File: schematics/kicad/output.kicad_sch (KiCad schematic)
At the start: 33 parts, among them J7 DE15_Socket_HighDensity, K1300 10uF, U1300 HM53461, U1301 HM53461, U1302 HM53461, U1303 HM53461, U1304 HM53461, U1305 HM53461, U1306 HM53461, U1307 HM53461, U1310 BT458, U1311 92.9405Mhz, U1312 10H101, U1313 10H131, U1314 10H350, U1315 LM385BZ-1.2, U1318 74F08

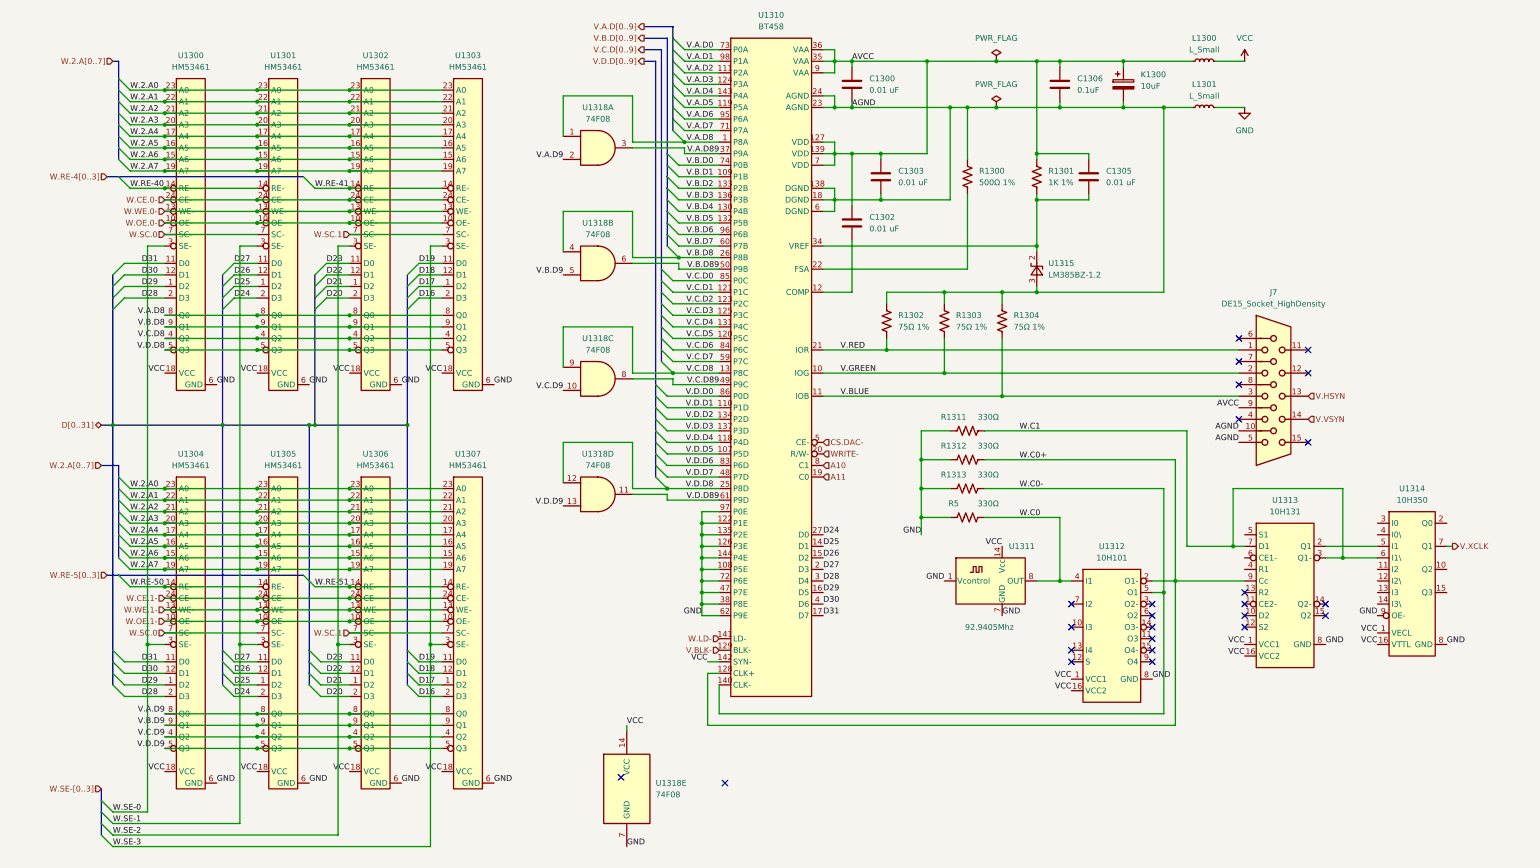
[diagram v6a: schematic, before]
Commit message: Fix ERCs which uncovered some issues with W.RE for the overlay memory. Finish the ECL chips for clock control - need to find value of R1315. Add space for 0-ohm resistor on V.VSYN which exists in schematics but was never connected in the original composite sync scheme with 4 BNC connectors. Can leave it unconnected if it causes issues.
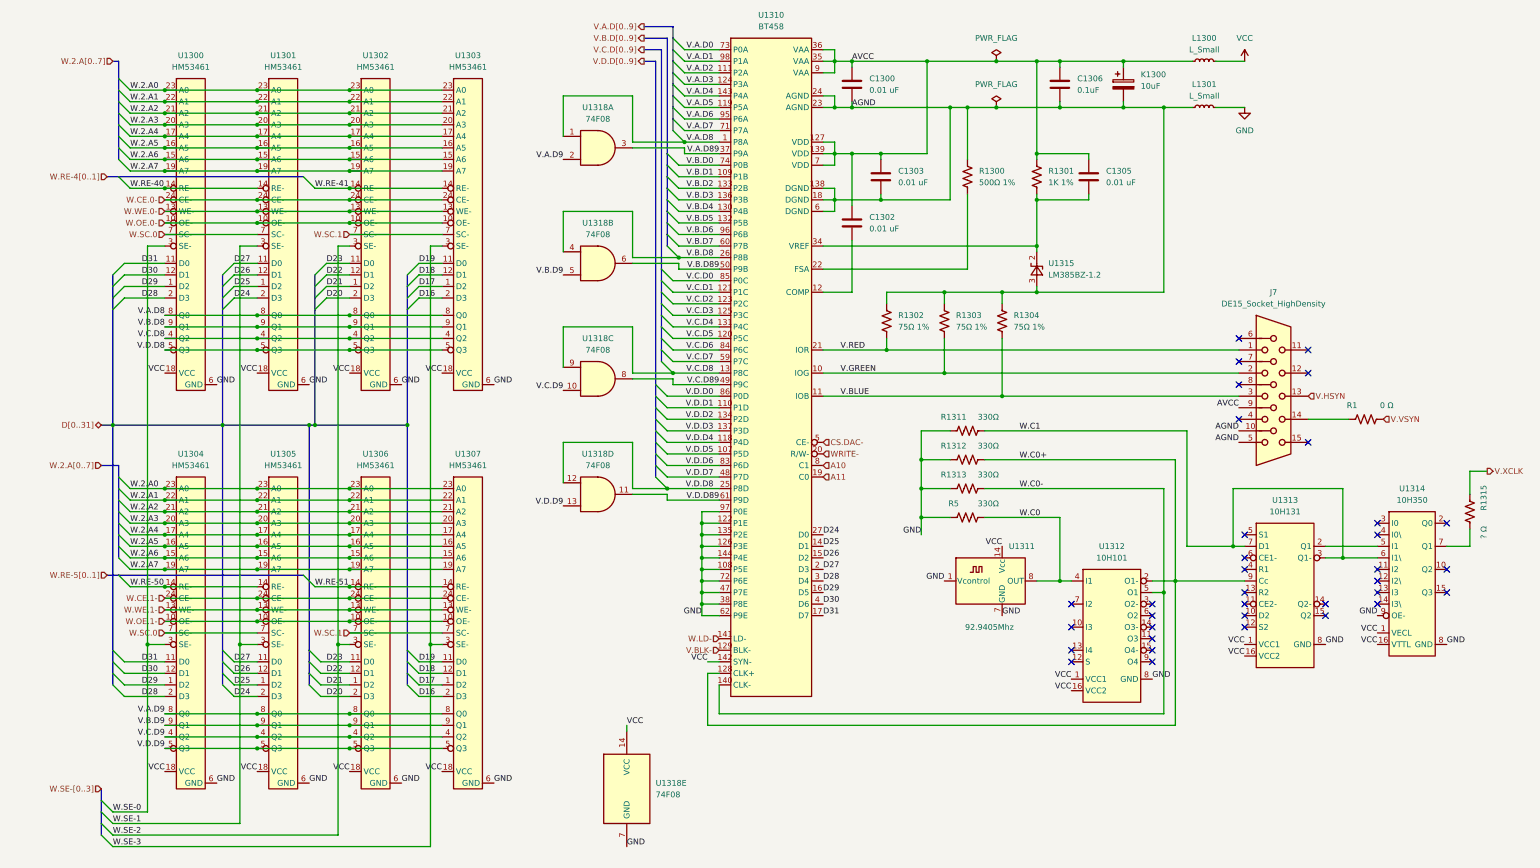
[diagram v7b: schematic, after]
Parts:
- added R1: 0 Ω, Resistor_THT:R_Axial_DIN0207_L6.3mm_D2.5mm_P10.16mm_Horizontal, symbol Device:R_US
- added R1315: ? Ω, Resistor_THT:R_Axial_DIN0207_L6.3mm_D2.5mm_P10.16mm_Horizontal, symbol Device:R_US
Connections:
- net V.VSYN: now also R1.2; no longer J7.14
- net V.XCLK: now also R1315.1; no longer U1314.7 (Q1)
- new net: R1315.2, U1314.7 (Q1)
- new net: J7.14, R1.1
- no-connect marks 25 -> 35
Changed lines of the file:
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@@
 	)
 	(no_connect
-		(at 166.37 182.88)
+		(at 280.67 146.05)
 	)
 	(no_connect
-		(at 280.67 146.05)
+		(at 280.67 135.89)
 	)
 	(no_connect
@@
 	)
 	(no_connect
+		(at 309.88 125.73)
+	)
+	(no_connect
+		(at 309.88 135.89)
+	)
+	(no_connect
+		(at 309.88 140.97)
+	)
+	(no_connect
 		(at 294.64 107.95)
 	)
@@
 	)
 	(no_connect
-		(at 294.64 87.63)
+		(at 309.88 143.51)
 	)
 	(no_connect
-		(at 143.51 181.61)
+		(at 294.64 87.63)
 	)
 	(no_connect
@@
 	)
 	(no_connect
+		(at 280.67 133.35)
+	)
+	(no_connect
 		(at 260.35 151.13)
 	)
@@
 	)
 	(no_connect
+		(at 325.12 125.73)
+	)
+	(no_connect
 		(at 242.57 156.21)
 	)
@@
 	)
 	(no_connect
+		(at 280.67 128.27)
+	)
+	(no_connect
+		(at 309.88 138.43)
+	)
+	(no_connect
 		(at 280.67 143.51)
 	)
@@
 	)
 	(no_connect
+		(at 309.88 128.27)
+	)
+	(no_connect
 		(at 242.57 143.51)
 	)
@@
 	)
 	(no_connect
+		(at 325.12 140.97)
+	)
+	(no_connect
+		(at 325.12 135.89)
+	)
+	(no_connect
 		(at 279.4 90.17)
 	)
@@
 	(wire
 		(pts
+			(xy 303.53 102.87) (xy 294.64 102.87)
+		)
+		(stroke
+			(width 0)
+			(type default)
+		)
+	)
+	(wire
+		(pts
 			(xy 63.5 170.18) (xy 83.82 170.18)
 		)
@@
 	(wire
 		(pts
-			(xy 325.12 130.81) (xy 326.39 130.81)
-		)
-		(stroke
-			(width 0)
-			(type default)
-		)
-	)
-	(wire
-		(pts
 			(xy 157.48 36.83) (xy 165.1 36.83)
 		)
@@
 	(wire
 		(pts
+			(xy 330.2 127) (xy 330.2 130.81)
+		)
+		(stroke
+			(width 0)
+			(type default)
+		)
+	)
+	(wire
+		(pts
 			(xy 43.18 52.07) (xy 63.5 52.07)
 		)
@@
 	(wire
 		(pts
+			(xy 330.2 114.3) (xy 330.2 119.38)
+		)
+		(stroke
+			(width 0)
+			(type default)
+		)
+	)
+	(wire
+		(pts
 			(xy 83.82 35.56) (xy 104.14 35.56)
 		)
@@
 		)
 	)
+	(wire
+		(pts
+			(xy 330.2 114.3) (xy 334.01 114.3)
+		)
+		(stroke
+			(width 0)
+			(type default)
+		)
+	)
 	(bus
 		(pts
@@
 	(wire
 		(pts
+			(xy 325.12 130.81) (xy 330.2 130.81)
+		)
+		(stroke
+			(width 0)
+			(type default)
+		)
+	)
+	(wire
+		(pts
 			(xy 153.67 107.95) (xy 165.1 107.95)
 		)
@@
 		)
 	)
-	(hierarchical_label "W.RE-4[0..3]"
+	(hierarchical_label "V.XCLK"
+		(shape output)
+		(at 334.01 114.3 0)
+		(effects
+			(font
+				(size 1.27 1.27)
+			)
+			(justify left)
+		)
+	)
+	(hierarchical_label "W.RE-4[0..1]"
 		(shape input)
 		(at 30.48 49.53 180)
@@
 		)
 	)
-	(hierarchical_label "V.XCLK"
-		(shape output)
-		(at 326.39 130.81 0)
+	(hierarchical_label "V.VSYN"
+		(shape input)
+		(at 311.15 102.87 0)
 		(effects
 			(font
@@
 		)
 	)
-	(hierarchical_label "V.VSYN"
-		(shape input)
-		(at 294.64 102.87 0)
-		(effects
-			(font
-				(size 1.27 1.27)
-			)
-			(justify left)
-		)
-	)
 	(hierarchical_label "A11"
 		(shape input)
@@
 		)
 	)
-	(hierarchical_label "W.RE-5[0..3]"
+	(hierarchical_label "W.RE-5[0..1]"
 		(shape input)
 		(at 30.48 137.16 180)
@@
 	)
 	(symbol
+		(lib_id "Device:R_US")
+		(at 330.2 123.19 0)
+		(unit 1)
+		(exclude_from_sim no)
+		(in_bom yes)
+		(on_board yes)
+		(dnp no)
+		(property "Reference" "R1315"
+			(at 333.248 120.142 90)
+			(effects
+				(font
+					(size 1.27 1.27)
+				)
+			)
+		)
+		(property "Value" "? Ω"
+			(at 333.248 127.762 90)
+			(effects
+				(font
+					(size 1.27 1.27)
+				)
+			)
+		)
+		(property "Footprint" "Resistor_THT:R_Axial_DIN0207_L6.3mm_D2.5mm_P10.16mm_Horizontal"
+			(at 331.216 123.444 90)
+			(effects
+				(font
+					(size 1.27 1.27)
+				)
+				(hide yes)
+			)
+		)
+		(property "Datasheet" "~"
+			(at 330.2 123.19 0)
+			(effects
+				(font
+					(size 1.27 1.27)
+				)
+				(hide yes)
+			)
+		)
+		(property "Description" "Resistor, US symbol"
+			(at 330.2 123.19 0)
+			(effects
+				(font
+					(size 1.27 1.27)
+				)
+				(hide yes)
+			)
+		)
+		(pin "2"
+		)
+		(pin "1"
+		)
+		(instances
+			(project "cg4"
+				(path "/7c2b6a13-c303-4adb-8eed-6e6a9ac5307e/29ede95e-baf3-44af-bd6e-b3be323fd399"
+					(reference "R1315")
+					(unit 1)
+				)
+			)
+		)
+	)
+	(symbol
 		(lib_id "power:PWR_FLAG")
 		(at 226.06 34.29 0)
@@
 					(unit 1)
 				)
+			)
+		)
+	)
+	(symbol
+		(lib_id "Device:R_US")
+		(at 307.34 102.87 90)
+		(unit 1)
+		(exclude_from_sim no)
+		(in_bom yes)
+		(on_board yes)
+		(dnp no)
+		(property "Reference" "R1"
+			(at 304.292 99.822 90)
+			(effects
+				(font
+					(size 1.27 1.27)
+				)
+			)
+		)
+		(property "Value" "0 Ω"
+			(at 311.912 99.822 90)
+			(effects
+				(font
+					(size 1.27 1.27)
+				)
+			)
+		)
+		(property "Footprint" "Resistor_THT:R_Axial_DIN0207_L6.3mm_D2.5mm_P10.16mm_Horizontal"
+			(at 307.594 101.854 90)
+			(effects
+				(font
+					(size 1.27 1.27)
+				)
+				(hide yes)
+			)
+		)
+		(property "Datasheet" "~"
+			(at 307.34 102.87 0)
+			(effects
+				(font
+					(size 1.27 1.27)
+				)
+				(hide yes)
+			)
+		)
+		(property "Description" "Resistor, US symbol"
+			(at 307.34 102.87 0)
+			(effects
+				(font
+					(size 1.27 1.27)
+				)
+				(hide yes)
+			)
+		)
+		(pin "2"
+		)
+		(pin "1"
+		)
+		(instances
+			(project "cg4"
+				(path "/7c2b6a13-c303-4adb-8eed-6e6a9ac5307e/29ede95e-baf3-44af-bd6e-b3be323fd399"
+					(reference "R1")
+					(unit 1)
+				)

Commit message: Finish routing and misc fixes in the analog section
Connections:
- net AGND: now also U1310.108 (P5E), U1310.122 (P1E), U1310.126 (P3E), U1310.135 (P2E), U1310.144 (P4E), U1310.38 (P8E), U1310.47 (P7E), U1310.62 (P9E), U1310.72 (P6E), U1310.97 (P0E)
- net AVCC: now also U1310.142 (SYN-)
- net GND: no longer U1310.108 (P5E), U1310.122 (P1E), U1310.126 (P3E), U1310.135 (P2E), U1310.144 (P4E), U1310.38 (P8E), U1310.47 (P7E), U1310.62 (P9E), U1310.72 (P6E), U1310.97 (P0E)
- net VCC: no longer U1310.142 (SYN-)
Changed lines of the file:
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@@
 		)
 	)
-	(label "GND"
+	(label "AGND"
 		(at 161.29 146.05 180)
 		(effects
@@
 		)
 	)
-	(label "VCC"
+	(label "AVCC"
 		(at 162.56 156.21 180)
 		(effects
